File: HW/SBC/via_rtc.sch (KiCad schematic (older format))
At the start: 11 parts, among them J2 VIA1PA, J3 VIA1PB, J7 VIA2PB, U12 WD65C22, U6 WD65C22, U7 DS1511Y+

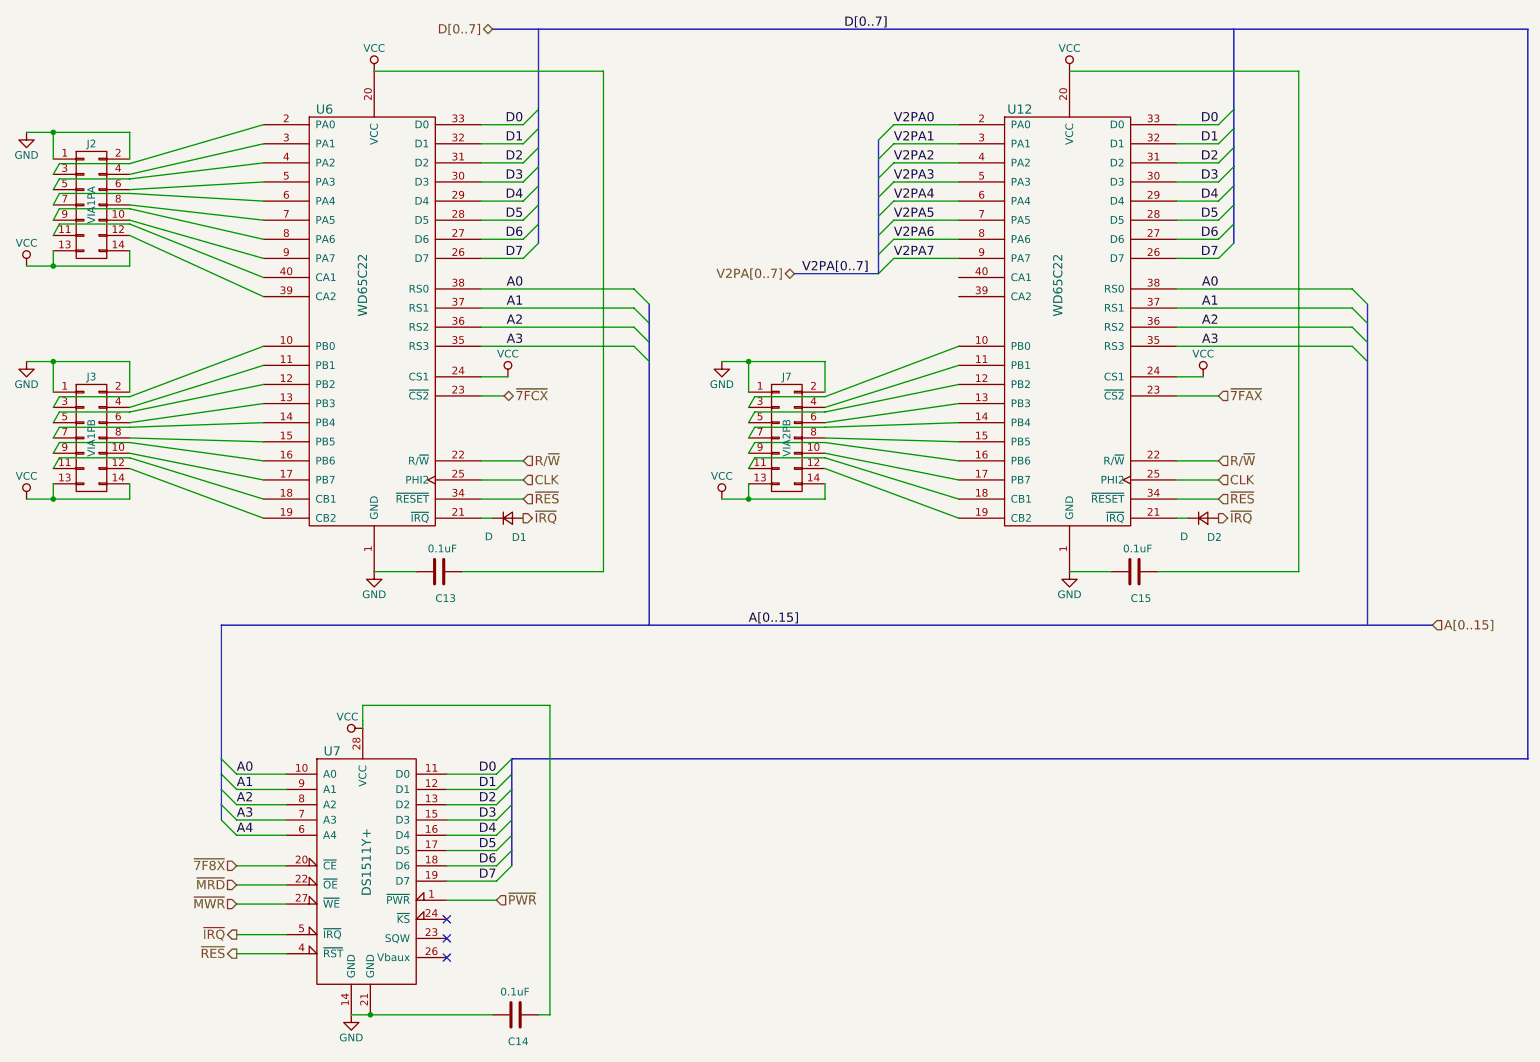
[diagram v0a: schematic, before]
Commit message: Connected most hierarchical labels between the sheets. Added a connector to AY IO port.
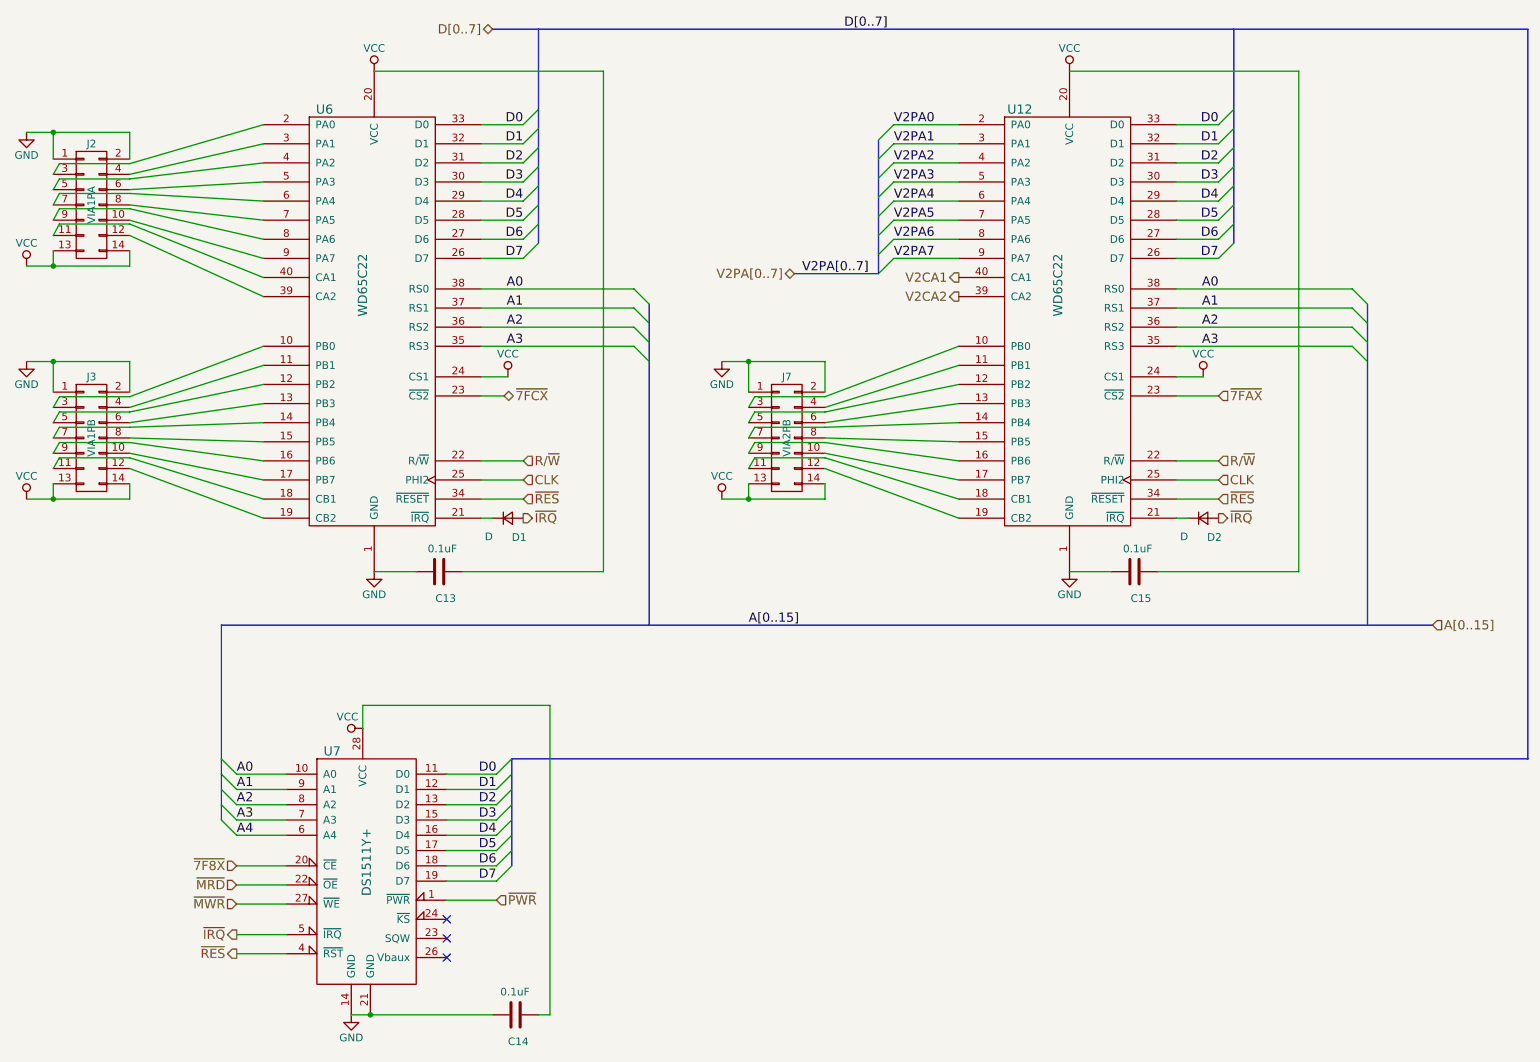
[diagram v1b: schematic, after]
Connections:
- net V2CA2: now reaches U12.39 (CA2)
- net V2CA1: now reaches U12.40 (CA1)
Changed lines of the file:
@@
 $EndComp
 $Comp
-L VCC #PWR22
+L VCC #PWR019
 U 1 1 58D69383
 P 700 3725
-F 0 "#PWR22" H 700 3575 50  0001 C CNN
+F 0 "#PWR019" H 700 3575 50  0001 C CNN
 F 1 "VCC" H 700 3875 50  0000 C CNN
 F 2 "" H 700 3725 50  0001 C CNN
@@
 $EndComp
 $Comp
-L GND #PWR21
+L GND #PWR020
 U 1 1 58D6939F
 P 700 2825
-F 0 "#PWR21" H 700 2575 50  0001 C CNN
+F 0 "#PWR020" H 700 2575 50  0001 C CNN
 F 1 "GND" H 700 2675 50  0000 C CNN
 F 2 "" H 700 2825 50  0001 C CNN
@@
 $EndComp
 $Comp
-L GND #PWR19
+L GND #PWR021
 U 1 1 58D6973D
 P 700 1325
-F 0 "#PWR19" H 700 1075 50  0001 C CNN
+F 0 "#PWR021" H 700 1075 50  0001 C CNN
 F 1 "GND" H 700 1175 50  0000 C CNN
 F 2 "" H 700 1325 50  0001 C CNN
@@
 $EndComp
 $Comp
-L VCC #PWR20
+L VCC #PWR022
 U 1 1 58D69759
 P 700 2200
-F 0 "#PWR20" H 700 2050 50  0001 C CNN
+F 0 "#PWR022" H 700 2050 50  0001 C CNN
 F 1 "VCC" H 700 2350 50  0000 C CNN
 F 2 "" H 700 2200 50  0001 C CNN
@@
 $EndComp
 $Comp
-L VCC #PWR27
+L VCC #PWR023
 U 1 1 58D6982A
 P 3850 2925
-F 0 "#PWR27" H 3850 2775 50  0001 C CNN
+F 0 "#PWR023" H 3850 2775 50  0001 C CNN
 F 1 "VCC" H 3850 3075 50  0000 C CNN
 F 2 "" H 3850 2925 50  0001 C CNN
@@
 	1375 3725 1375 3625
 Wire Wire Line
-	700  3725 875  3725
-Wire Wire Line
-	875  3725 1375 3725
+	700  3725 1375 3725
 Wire Wire Line
 	875  3725 875  3625
@@
 	1375 2825 1375 3025
 Wire Wire Line
-	700  2825 875  2825
-Wire Wire Line
-	875  2825 1375 2825
+	700  2825 1375 2825
 Wire Wire Line
 	875  2825 875  3025
@@
 	1375 2200 1375 2100
 Wire Wire Line
-	700  2200 875  2200
-Wire Wire Line
-	875  2200 1375 2200
+	700  2200 1375 2200
 Wire Wire Line
 	875  2200 875  2100
@@
 	1375 1325 1375 1500
 Wire Wire Line
-	700  1325 875  1325
-Wire Wire Line
-	875  1325 1375 1325
+	700  1325 1375 1325
 Wire Wire Line
 	875  1325 875  1500
@@
 	3450 5625 3775 5625
 Wire Wire Line
-	2825 7100 2950 7100
-Wire Wire Line
-	2950 7100 3750 7100
+	2825 7100 3750 7100
 Wire Wire Line
 	3450 6350 3775 6350
@@
 Connection ~ 2950 7100
 Wire Wire Line
-	2900 5225 2900 5200
-Wire Wire Line
-	2900 5200 2900 5175
+	2900 5075 2900 5225
 Wire Wire Line
 	4050 7100 4125 7100
@@
 	4125 7100 4125 5075
 Wire Wire Line
-	4125 5075 3150 5075
-Wire Wire Line
-	3150 5075 2900 5075
-Wire Wire Line
-	2900 5075 2900 5175
+	4125 5075 2900 5075
 Wire Wire Line
 	4475 925  2975 925
 $Comp
-L VCC #PWR25
+L VCC #PWR024
 U 1 1 5924C298
 P 2975 925
-F 0 "#PWR25" H 2975 775 50  0001 C CNN
+F 0 "#PWR024" H 2975 775 50  0001 C CNN
 F 1 "VCC" H 2975 1075 50  0000 C CNN
 F 2 "" H 2975 925 50  0001 C CNN
@@
 $EndComp
 $Comp
-L GND #PWR26
+L GND #PWR025
 U 1 1 5924C3BB
 P 2975 4200
-F 0 "#PWR26" H 2975 3950 50  0001 C CNN
+F 0 "#PWR025" H 2975 3950 50  0001 C CNN
 F 1 "GND" H 2975 4050 50  0000 C CNN
 F 2 "" H 2975 4200 50  0001 C CNN
@@
 $EndComp
 $Comp
-L VCC #PWR24
+L VCC #PWR026
 U 1 1 5924C55A
 P 2900 5225
-F 0 "#PWR24" H 2900 5075 50  0001 C CNN
+F 0 "#PWR026" H 2900 5075 50  0001 C CNN
 F 1 "VCC" V 2975 5325 50  0000 C CNN
 F 2 "" H 2900 5225 50  0001 C CNN
@@
 $EndComp
 $Comp
-L GND #PWR23
+L GND #PWR027
 U 1 1 5924C775
 P 2825 7100
-F 0 "#PWR23" H 2825 6850 50  0001 C CNN
+F 0 "#PWR027" H 2825 6850 50  0001 C CNN
 F 1 "GND" H 2825 6950 50  0000 C CNN
 F 2 "" H 2825 7100 50  0001 C CNN
@@
 $EndComp
 $Comp
-L VCC #PWR29
+L VCC #PWR028
 U 1 1 5930635F
 P 5250 3725
-F 0 "#PWR29" H 5250 3575 50  0001 C CNN
+F 0 "#PWR028" H 5250 3575 50  0001 C CNN
 F 1 "VCC" H 5250 3875 50  0000 C CNN
 F 2 "" H 5250 3725 50  0001 C CNN
@@
 $EndComp
 $Comp
-L GND #PWR28
+L GND #PWR029
 U 1 1 59306365
 P 5250 2825
-F 0 "#PWR28" H 5250 2575 50  0001 C CNN
+F 0 "#PWR029" H 5250 2575 50  0001 C CNN
 F 1 "GND" H 5250 2675 50  0000 C CNN
 F 2 "" H 5250 2825 50  0001 C CNN
@@
 $EndComp
 $Comp
-L VCC #PWR32
+L VCC #PWR030
 U 1 1 59306377
 P 8400 2925
-F 0 "#PWR32" H 8400 2775 50  0001 C CNN
+F 0 "#PWR030" H 8400 2775 50  0001 C CNN
 F 1 "VCC" H 8400 3075 50  0000 C CNN
 F 2 "" H 8400 2925 50  0001 C CNN
@@
 	5925 3725 5925 3625
 Wire Wire Line
-	5250 3725 5425 3725
-Wire Wire Line
-	5425 3725 5925 3725
+	5250 3725 5925 3725
 Wire Wire Line
 	5425 3725 5425 3625
@@
 	5925 2825 5925 3025
 Wire Wire Line
-	5250 2825 5425 2825
-Wire Wire Line
-	5425 2825 5925 2825
+	5250 2825 5925 2825
 Wire Wire Line
 	5425 2825 5425 3025
@@
 	9025 925  7525 925
 $Comp
-L VCC #PWR30
+L VCC #PWR031
 U 1 1 593063DC
 P 7525 925
-F 0 "#PWR30" H 7525 775 50  0001 C CNN
+F 0 "#PWR031" H 7525 775 50  0001 C CNN
 F 1 "VCC" H 7525 1075 50  0000 C CNN
 F 2 "" H 7525 925 50  0001 C CNN
@@
 $EndComp
 $Comp
-L GND #PWR31
+L GND #PWR032
 U 1 1 593063E2
 P 7525 4200
-F 0 "#PWR31" H 7525 3950 50  0001 C CNN
+F 0 "#PWR032" H 7525 3950 50  0001 C CNN
 F 1 "GND" H 7525 4050 50  0000 C CNN
 F 2 "" H 7525 4200 50  0001 C CNN
@@
 	6275 2250 6375 2150
 Wire Bus Line
-	6275 1375 6275 1500
-Wire Bus Line
-	6275 1500 6275 1625
-Wire Bus Line
-	6275 1625 6275 1750
-Wire Bus Line
-	6275 1750 6275 1875
-Wire Bus Line
-	6275 1875 6275 2000
-Wire Bus Line
-	6275 2000 6275 2125
-Wire Bus Line
-	6275 2125 6275 2250
+	6275 1375 6275 2250
 Wire Bus Line
 	6275 2250 5725 2250
@@
 	3950 2150 4050 2050
 Wire Bus Line
-	4050 650  4050 1175
-Wire Bus Line
-	4050 1175 4050 1300
-Wire Bus Line
-	4050 1300 4050 1425
-Wire Bus Line
-	4050 1425 4050 1550
-Wire Bus Line
-	4050 1550 4050 1675
-Wire Bus Line
-	4050 1675 4050 1800
-Wire Bus Line
-	4050 1800 4050 1925
-Wire Bus Line
-	4050 1925 4050 2050
+	4050 650  4050 2050
 Wire Bus Line
 	3750 650  10525 650
 Wire Bus Line
-	8600 650  8600 1175
-Wire Bus Line
-	8600 1175 8600 1300
-Wire Bus Line
-	8600 1300 8600 1425
-Wire Bus Line
-	8600 1425 8600 1550
-Wire Bus Line
-	8600 1550 8600 1675
-Wire Bus Line
-	8600 1675 8600 1800
-Wire Bus Line
-	8600 1800 8600 1925
-Wire Bus Line
-	8600 1925 8600 2050
+	8600 650  8600 2050
 Text Label 6050 650  0    60   ~ 0
 D[0..7]
@@
 	9375 2350 9475 2450
 Wire Bus Line
-	9475 2450 9475 2575
-Wire Bus Line
-	9475 2575 9475 2700
-Wire Bus Line
-	9475 2700 9475 2825
-Wire Bus Line
-	9475 2825 9475 4550
+	9475 2450 9475 4550
 Wire Bus Line
 	1975 4550 9900 4550
 Wire Bus Line
-	4775 2450 4775 2575
-Wire Bus Line
-	4775 2575 4775 2700
-Wire Bus Line
-	4775 2700 4775 2825
-Wire Bus Line
-	4775 2825 4775 4550
+	4775 2450 4775 4550
 Text Label 5425 4550 0    60   ~ 0
 A[0..15]
@@
 	10525 5425 3875 5425
 Wire Bus Line
-	3875 5425 3875 5525
-Wire Bus Line
-	3875 5525 3875 5625
-Wire Bus Line
-	3875 5625 3875 5725
-Wire Bus Line
-	3875 5725 3875 5825
-Wire Bus Line
-	3875 5825 3875 5925
-Wire Bus Line
-	3875 5925 3875 6025
-Wire Bus Line
-	3875 6025 3875 6125
+	3875 5425 3875 6125
 Wire Wire Line
 	2400 5525 2075 5525
@@
 	1975 5825 2075 5925
 Wire Bus Line
-	1975 4550 1975 5425
-Wire Bus Line
-	1975 5425 1975 5525
-Wire Bus Line
-	1975 5525 1975 5625
-Wire Bus Line
-	1975 5625 1975 5725
-Wire Bus Line
-	1975 5725 1975 5825
+	1975 4550 1975 5825
 Text HLabel 3775 6350 2    60   Input ~ 0
 ~PWR
@@
 Text HLabel 3950 3850 2    60   Output ~ 0
 ~IRQ
+Text HLabel 6800 2275 0    60   Output ~ 0
+V2CA1
+Text HLabel 6800 2400 0    60   Output ~ 0
+V2CA2
 $EndSCHEMATC

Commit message: Still no VCC net in PCBnew.
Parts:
- U12, U6: footprint Housings_DIP:DIP-40_W15.24mm -> Housings_DIP:DIP-40_W15.24mm_Socket
- U7: footprint Housings_DIP:DIP-28_W15.24mm -> Housings_DIP:DIP-28_W15.24mm_Socket
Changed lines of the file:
@@
 EESchema Schematic File Version 2
-LIBS:pluto-rescue
 LIBS:power
 LIBS:device
@@
 LIBS:pluto
 LIBS:pluto-cache
-LIBS:IDE_interface-cache
 EELAYER 25 0
 EELAYER END
@@
 F 0 "U6" H 2650 3275 60  0000 C CNN
 F 1 "WD65C22" V 2900 2125 60  0000 C CNN
-F 2 "Housings_DIP:DIP-40_W15.24mm" H 2400 2425 60  0001 C CNN
+F 2 "Housings_DIP:DIP-40_W15.24mm_Socket" H 2400 2425 60  0001 C CNN
 F 3 "" H 2400 2425 60  0000 C CNN
 	1    2900 2225
@@
 F 0 "U7" H 2700 6825 60  0000 C CNN
 F 1 "DS1511Y+" V 2925 6100 60  0000 C CNN
-F 2 "Housings_DIP:DIP-28_W15.24mm" H 2625 6550 60  0001 C CNN
+F 2 "Housings_DIP:DIP-28_W15.24mm_Socket" H 2625 6550 60  0001 C CNN
 F 3 "" H 2625 6550 60  0001 C CNN
 	1    2875 6100
@@
 F 0 "U12" H 7200 3275 60  0000 C CNN
 F 1 "WD65C22" V 7450 2125 60  0000 C CNN
-F 2 "Housings_DIP:DIP-40_W15.24mm" H 6950 2425 60  0001 C CNN
+F 2 "Housings_DIP:DIP-40_W15.24mm_Socket" H 6950 2425 60  0001 C CNN
 F 3 "" H 6950 2425 60  0000 C CNN
 	1    7450 2225

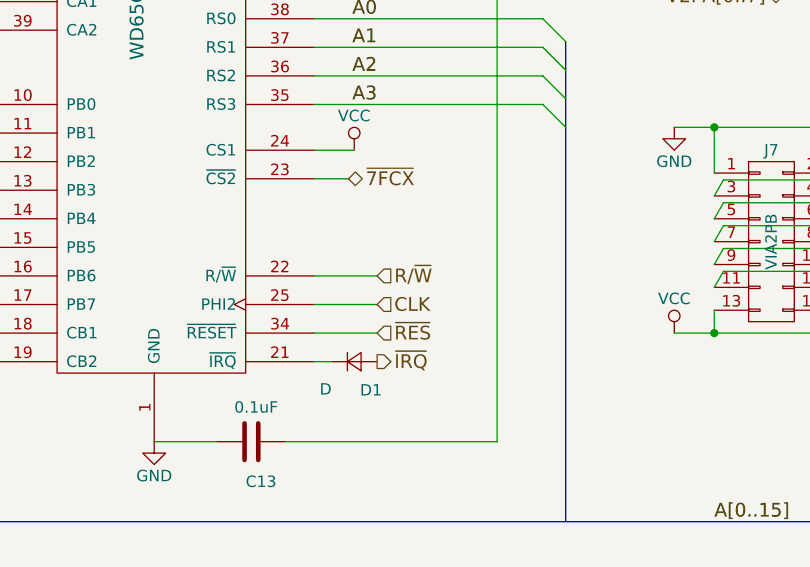
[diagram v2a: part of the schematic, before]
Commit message: New PCB layout. Added datasheet for AY-3-8912 and LM386.
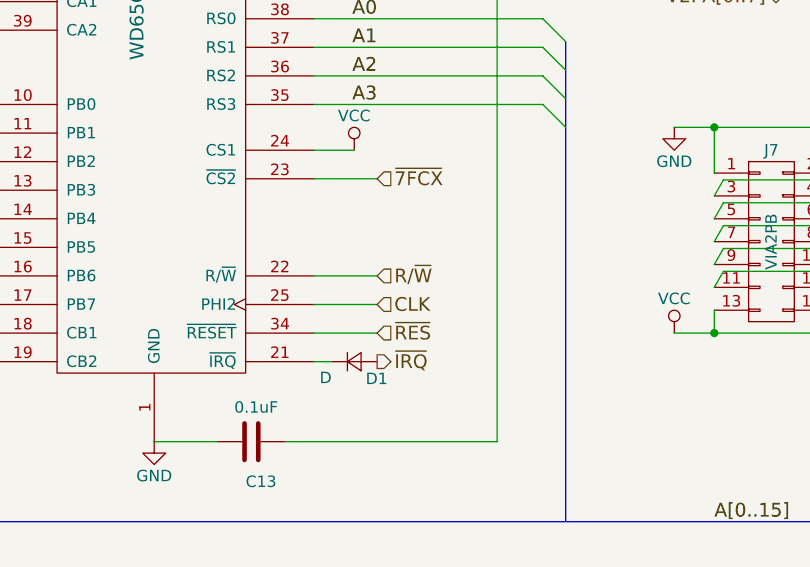
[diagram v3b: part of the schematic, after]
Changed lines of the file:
@@
 U 1 1 58D69B92
 P 3850 3850
-F 0 "D1" H 3875 3725 50  0000 L CNN
-F 1 "D" H 3725 3700 50  0000 C BNN
+F 0 "D1" H 3900 3775 50  0000 L CNN
+F 1 "D" H 3725 3750 50  0000 C BNN
 F 2 "Diodes_ThroughHole:D_DO-35_SOD27_P7.62mm_Horizontal" V 3850 3850 50  0001 C CNN
 F 3 "" V 3850 3850 50  0001 C CNN
@@
 	3675 2925 3850 2925
 Wire Wire Line
-	3675 3050 3825 3050
+	3675 3050 3950 3050
 Wire Wire Line
 	3675 3475 3950 3475
@@
 Text Label 3950 2725 2    60   ~ 0
 A3
-Text HLabel 3825 3050 2    60   BiDi ~ 0
+Text HLabel 3950 3050 2    60   Input ~ 0
 ~7FCX
 Text Label 8500 2350 2    60   ~ 0

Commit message: Schema is now Alpha.
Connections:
- net GND: now also U7.26 (Vbaux)
- net ~KS: now reaches U7.24 (~KS)
- no-connect marks 3 -> 1

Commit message: Initialisation routines developed. New library preferences to KiCad schema. Broken though but it doesn't matter as the PCB has been manufactured. Schema and PCB doesn't match 100% (e.g. 74HCT74 unused inputs are not grounded on PCB but are in schema).
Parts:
- U12, U6: symbol WD65C22 -> WD65C22-RESCUE-pluto
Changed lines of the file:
@@
 LIBS:uln-ic
 LIBS:IDE_interface
-LIBS:+1.8V
-LIBS:+3.3V
-LIBS:+5V
-LIBS:+9V
-LIBS:25AA02EXXX-XOT
-LIBS:74LVC8T245
-LIBS:4021
-LIBS:7408
-LIBS:74125
-LIBS:74138
-LIBS:74148
-LIBS:74151
-LIBS:74157
-LIBS:74541
-LIBS:ANT
-LIBS:AP6502
-LIBS:AUDIO-JACK-3
-LIBS:AUDIO-JACK-6
-LIBS:BATTERY
-LIBS:BELFUSE-08B0-1X1T-06-F
-LIBS:C
-LIBS:CP
-LIBS:CRYSTAL
-LIBS:CRYSTAL-14
-LIBS:CVAR
-LIBS:DIODE
-LIBS:DIODES-AP3211
-LIBS:DIODESCH
-LIBS:DIODEZENER
-LIBS:DMMT5401
-LIBS:EDISON-BULB-E10
-LIBS:EDISON-SOCKET-E10
-LIBS:ENC28J60
-LIBS:FTDI-PLUG
-LIBS:GNDPWR
-LIBS:~GNDPWR
-LIBS:INDUCTOR
-LIBS:INTEL-EDISON-COMPUTE-MODULE
-LIBS:IS31AP4066D
-LIBS:JTAG
-LIBS:JTAG10
-LIBS:LATTICE-LC4256
-LIBS:LED
-LIBS:LED-BI
-LIBS:LED-BI-COMMON-CATHODE
-LIBS:LM324
-LIBS:LM1875
-LIBS:MAX3221
-LIBS:MC33926
-LIBS:MC34063A
-LIBS:MCP49X1
-LIBS:MCP3204
-LIBS:MECH
-LIBS:MIC2039
-LIBS:MIC2288
-LIBS:MICROSD-AMPHENOL-114-00841-68
-LIBS:MOSFET-N
-LIBS:MOSFET-N-123
-LIBS:MOSFET-N-134
-LIBS:MOSFET-P
-LIBS:NPN
-LIBS:nRF8001
-LIBS:NXPUDA1334ATS
-LIBS:OPAMP-DUAL
-LIBS:P01
-LIBS:P02
-LIBS:P03
-LIBS:P05
-LIBS:P06
-LIBS:P06-MOTOR
-LIBS:P08
-LIBS:P10
-LIBS:P22
-LIBS:P24
-LIBS:PHOTO_TRANSISTOR
-LIBS:PIEZO
-LIBS:PNP
-LIBS:POLYFUSE
-LIBS:POT
-LIBS:PWR_FLAG
-LIBS:QRE1113
-LIBS:R
-LIBS:RASPBERRYPI
-LIBS:RASPBERRYPI2
-LIBS:RBUS8
-LIBS:RN4020
-LIBS:ROBOT-P10-IO
-LIBS:RS-232-DB-9-DTE
-LIBS:SEN-SHT3x-DIS
-LIBS:SERVO
-LIBS:SI4737-C40-GM
-LIBS:SI4737-GU
-LIBS:SKYWORKS-AAT1217-3.3
-LIBS:SPDT
-LIBS:SPST
-LIBS:SPST-4PIN
-LIBS:SST25VF032B-S2A
-LIBS:SST26VF032B
-LIBS:ST-LIS3MDL
-LIBS:STM32-32PIN
-LIBS:STM32-48PIN
-LIBS:STM32-64PIN
-LIBS:STM32SWDUART
-LIBS:ST-SWD
-LIBS:ST-TDA7266
-LIBS:SWD
-LIBS:TCS3472
-LIBS:TI-ADS7866
-LIBS:TICC3000
-LIBS:TIREF30XX
-LIBS:TP
-LIBS:TS5A623157
-LIBS:TSV631
-LIBS:TVS-DIODE
-LIBS:TXB0108-PW
-LIBS:USBAB
-LIBS:Vcc
-LIBS:Vdd
-LIBS:VIN
-LIBS:VREG
-LIBS:VREG_VOUTCENTER
 LIBS:74xgxx
 LIBS:ac-dc
@@
 $EndDescr
 $Comp
-L WD65C22 U6
+L WD65C22-RESCUE-pluto U6
 U 1 1 58D61E90
 P 2900 2225
@@
 $EndComp
 $Comp
-L WD65C22 U12
+L WD65C22-RESCUE-pluto U12
 U 1 1 59306341
 P 7450 2225
